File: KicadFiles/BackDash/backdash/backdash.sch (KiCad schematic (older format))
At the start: 7 parts

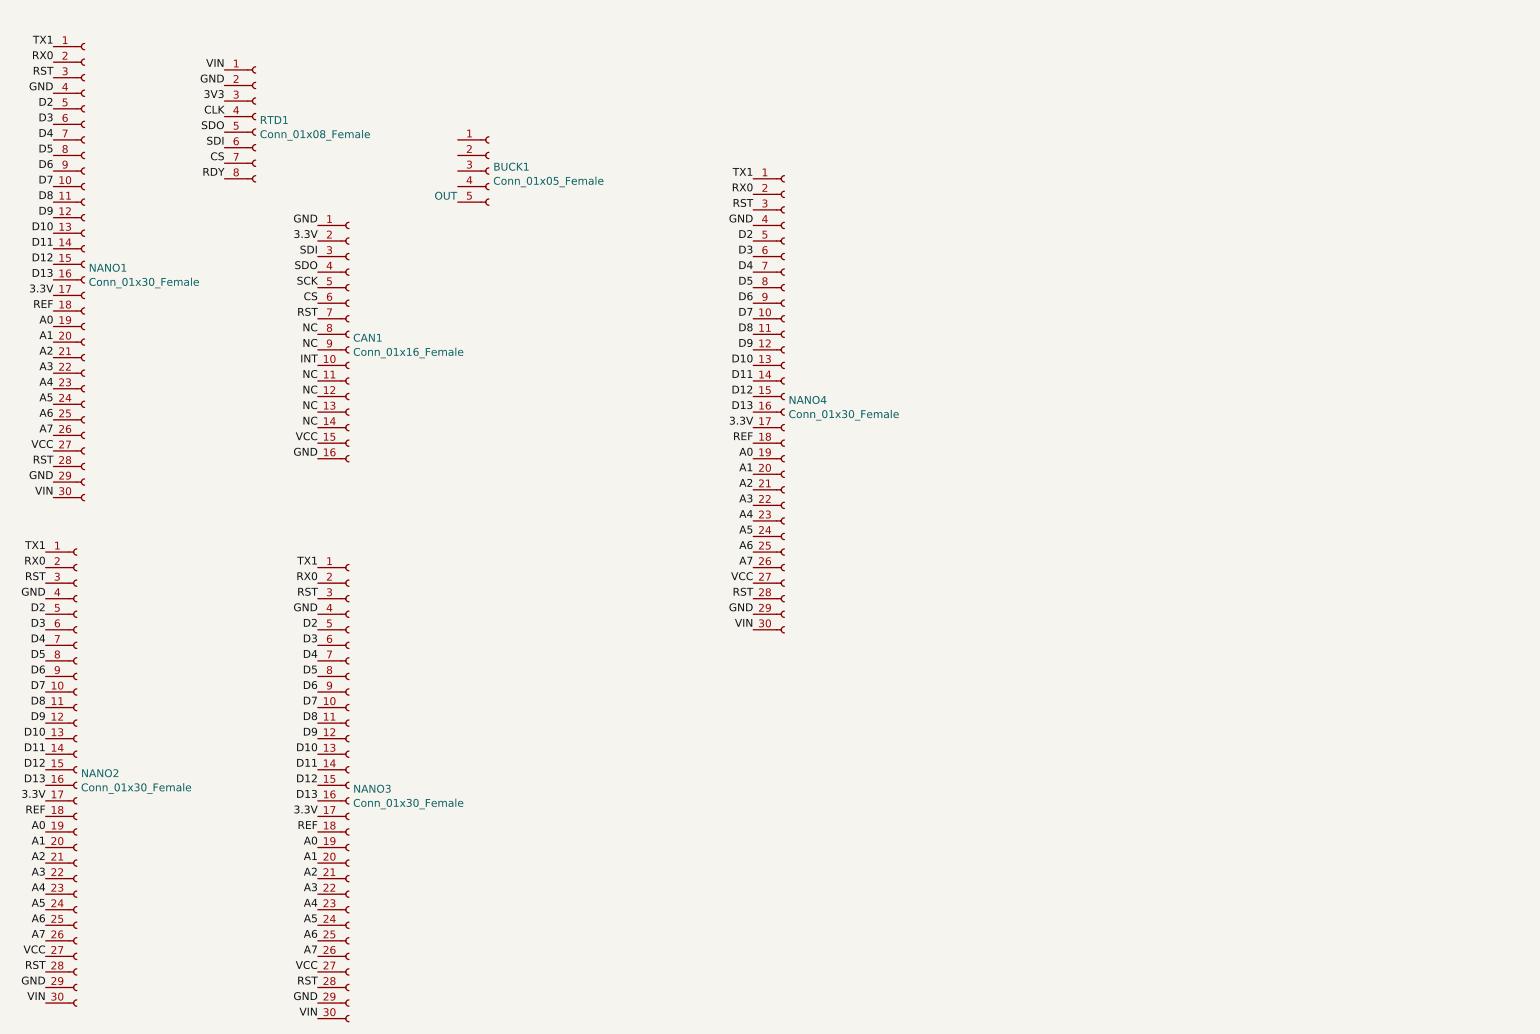
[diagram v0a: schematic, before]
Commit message: added tach sechematic, needs buck footprint
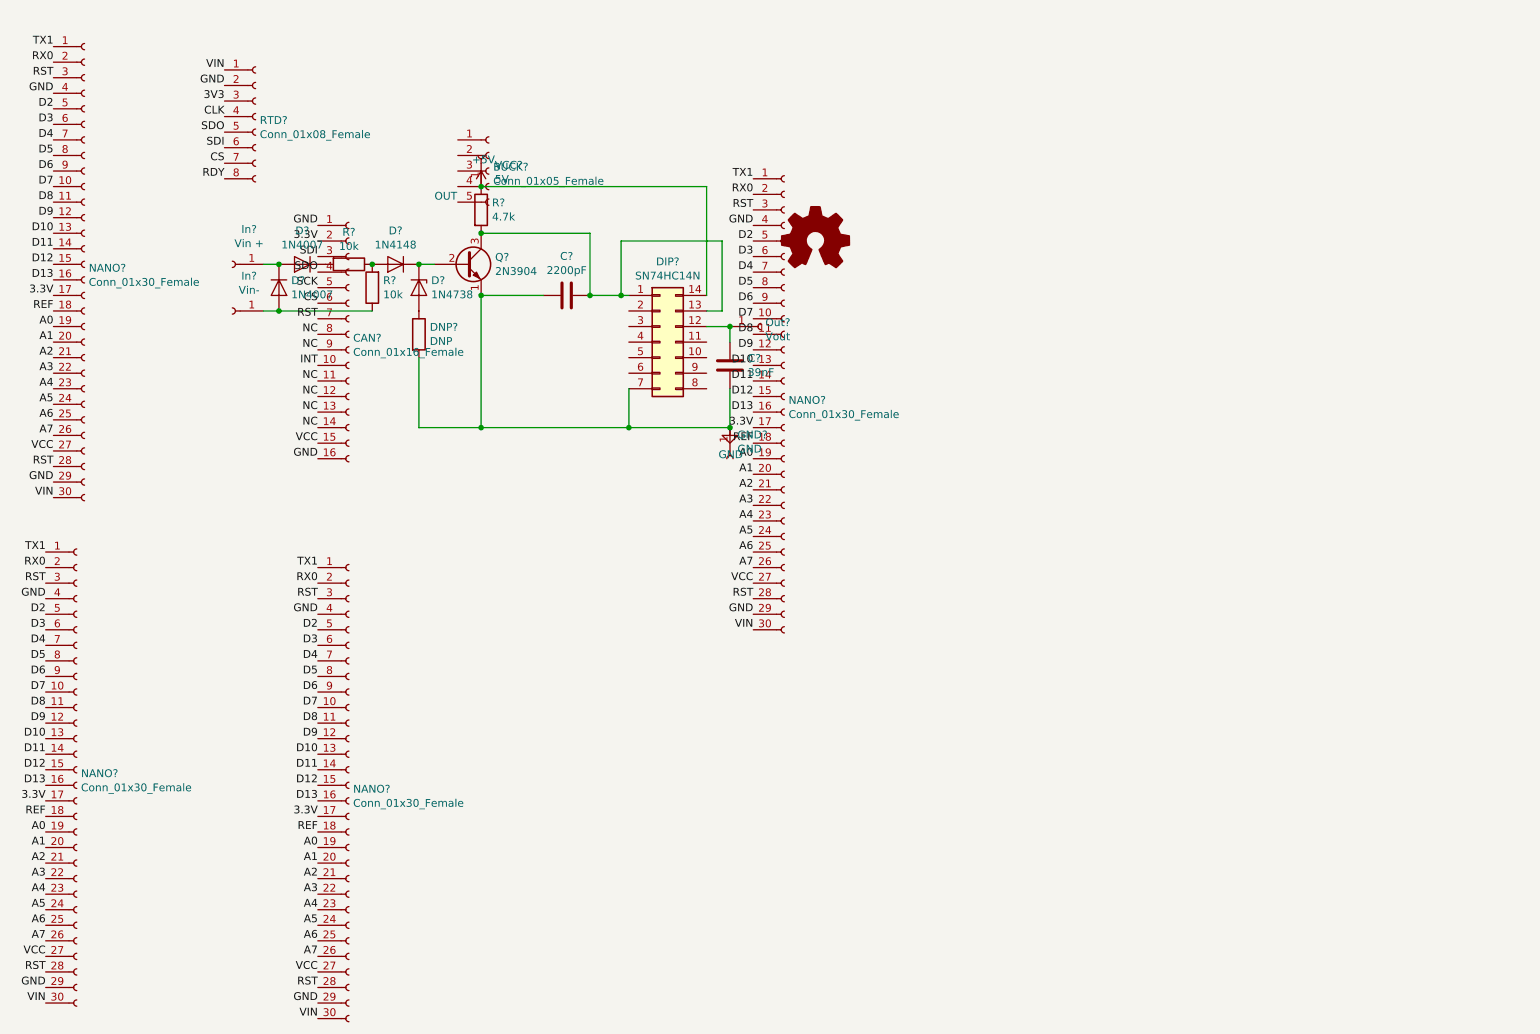
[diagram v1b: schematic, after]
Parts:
- added C?: 2200pF, Capacitor_THT:C_Rect_L11.0mm_W3.5mm_P10.00mm_MKT, symbol Device:C
- added C?: 39nF, Capacitor_THT:C_Rect_L7.0mm_W3.5mm_P5.00mm, symbol Device:C
- added D? (x2): 1N4007, Diode_THT:D_DO-41_SOD81_P7.62mm_Horizontal, symbol Diode:1N4007
- added D?: 1N4148, Diode_THT:D_T-1_P5.08mm_Horizontal, symbol Diode:1N4148
- added D?: 1N4738, Diode_THT:D_DO-41_SOD81_P7.62mm_Horizontal, symbol Diode:1N47xxA
- added DIP?: SN74HC14N, Package_DIP:DIP-14_W7.62mm, symbol Connector_Generic:Conn_02x07_Counter_Clockwise
- added DNP?: DNP, Resistor_SMD:R_0805_2012Metric, symbol Device:R
- added GND?: GND, Connector_PinHeader_2.54mm:PinHeader_1x02_P2.54mm_Vertical, symbol Connector:Conn_01x01_Female
- added In?: Vin-, Connector_PinHeader_2.54mm:PinHeader_1x02_P2.54mm_Vertical, symbol Connector:Conn_01x01_Female
- added In?: Vin +, Connector_PinHeader_2.54mm:PinHeader_1x02_P2.54mm_Vertical, symbol Connector:Conn_01x01_Female
- added Out?: Vout, Connector_PinHeader_2.54mm:PinHeader_1x02_P2.54mm_Vertical, symbol Connector:Conn_01x01_Female
- added Q?: 2N3904, Package_TO_SOT_THT:TO-92_Inline, symbol Transistor_BJT:2N3904
- added R? (x2): 10k, Resistor_SMD:R_0805_2012Metric, symbol Device:R
- added R?: 4.7k, Resistor_SMD:R_0805_2012Metric, symbol Device:R
- added VCC?: 5V, Connector_PinHeader_2.54mm:PinHeader_1x02_P2.54mm_Vertical, symbol Connector:Conn_01x01_Female
- renumbered BUCK1 to BUCK?, CAN1 to CAN?, NANO1 to NANO?, NANO4 to NANO?, NANO2 to NANO?, NANO3 to NANO?, RTD1 to RTD?
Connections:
- net GND: now also C?.2, C?.2, DIP?.7 (Pin_7), DNP?.2, GND?.1 (Pin_1), Q?.1 (E)
- new net: D?.1 (K), D?.2 (A), In?.1 (Pin_1)
- new net: D?.2 (A), In?.1 (Pin_1), R?.1
- new net: D?.1 (K), R?.2
- new net: D?.2 (A), R?.1, R?.2
- new net: D?.1 (K), D?.1 (K), Q?.2 (B)
- new net: D?.2 (A), DNP?.1
- new net: C?.1, DIP?.1 (Pin_1), DIP?.13 (Pin_13), Q?.3 (C), R?.2
- new net: C?.1, DIP?.12 (Pin_12), Out?.1 (Pin_1)
- new net +5V: DIP?.14 (Pin_14), R?.1, VCC?.1 (Pin_1)

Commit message: pcb is once again messy
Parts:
- removed GND?: GND, Connector_PinHeader_2.54mm:PinHeader_1x02_P2.54mm_Vertical, symbol Connector:Conn_01x01_Female
- removed Out?: Vout, Connector_PinHeader_2.54mm:PinHeader_1x02_P2.54mm_Vertical, symbol Connector:Conn_01x01_Female
- removed RTD?: Conn_01x08_Female, TestBaja:RTD, symbol Connector:Conn_01x08_Female
- removed VCC?: 5V, Connector_PinHeader_2.54mm:PinHeader_1x02_P2.54mm_Vertical, symbol Connector:Conn_01x01_Female
- gave numbers to parts that had none: 20
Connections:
- net +5V is gone; now on net VCC: DIP1.14 (Pin_14), R3.1
- net A0: now also C2.1, DIP1.12 (Pin_12)
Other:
- moved on the sheet: C1, C2, D1, D2, D3, D4, DIP1, DNP1, In1, In2, Q1, R1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
